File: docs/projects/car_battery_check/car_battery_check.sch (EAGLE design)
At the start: 18 parts, among them IC1 7805T, IC2 MEGA8-P

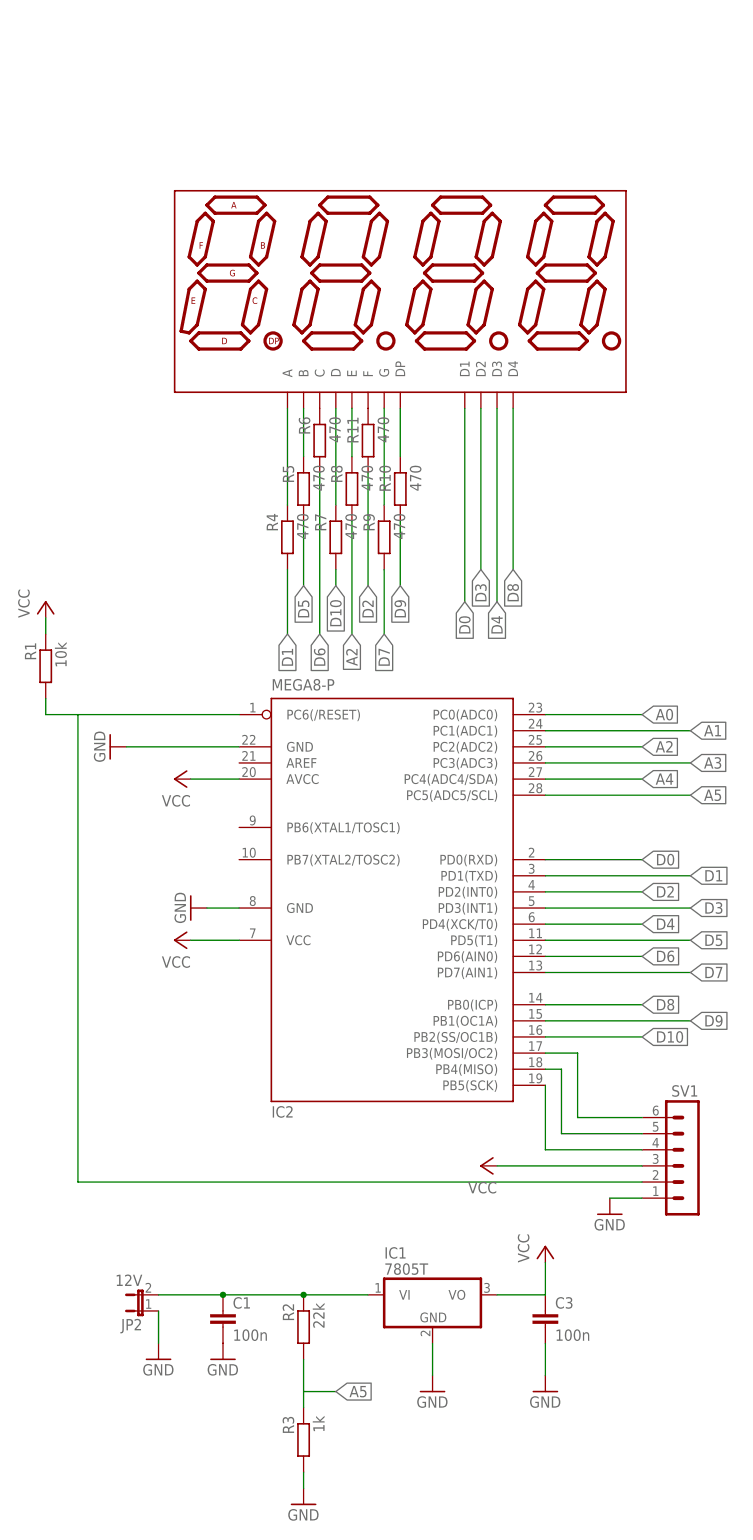
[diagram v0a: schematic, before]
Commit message: carbattery: adding voltage reference (MC1541)
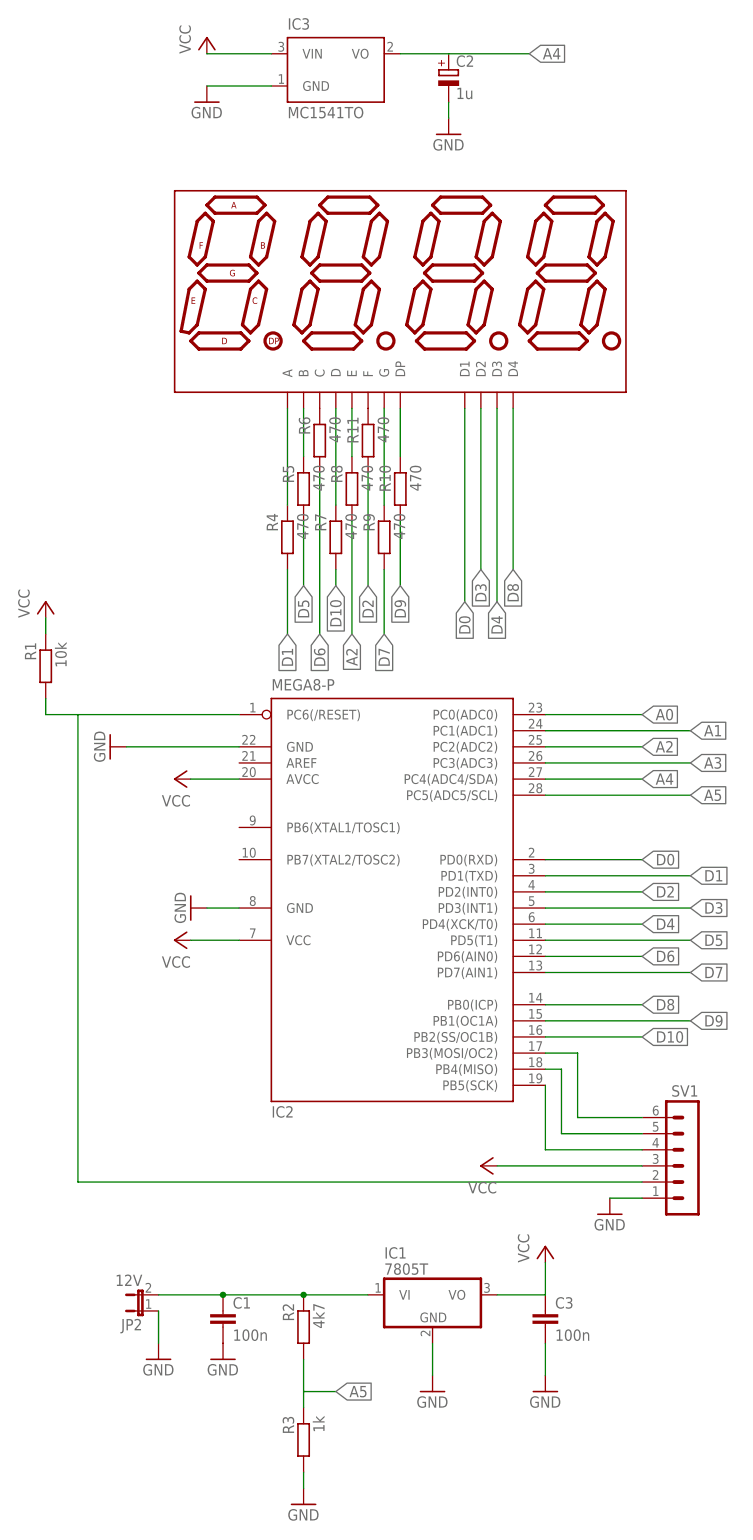
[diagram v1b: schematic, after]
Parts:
- added C2: 1u, rcl:CPOL-EUE2,5-6E
- added IC3: MC1541TO, microchip:MC1541TO
- R2: value 22k -> 4k7
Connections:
- net A4: now also C2.+, IC3.VO
- net GND: now also C2.-, IC3.GND
- net VCC: now also IC3.VIN
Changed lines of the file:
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@@
 <?xml version="1.0" encoding="utf-8"?>
 <!DOCTYPE eagle SYSTEM "eagle.dtd">
-<eagle version="6.2">
+<eagle version="6.4">
 <drawing>
 <settings>
@@
 <grid distance="0.1" unitdist="inch" unit="inch" style="lines" multiple="1" display="no" altdistance="0.01" altunitdist="inch" altunit="inch"/>
 <layers>
-<layer number="1" name="Top" color="4" fill="1" visible="yes" active="no"/>
-<layer number="16" name="Bottom" color="1" fill="1" visible="yes" active="no"/>
-<layer number="17" name="Pads" color="2" fill="1" visible="yes" active="no"/>
-<layer number="18" name="Vias" color="2" fill="1" visible="yes" active="no"/>
-<layer number="19" name="Unrouted" color="6" fill="1" visible="yes" active="no"/>
-<layer number="20" name="Dimension" color="15" fill="1" visible="yes" active="no"/>
-<layer number="21" name="tPlace" color="7" fill="1" visible="yes" active="no"/>
-<layer number="22" name="bPlace" color="7" fill="1" visible="yes" active="no"/>
-<layer number="23" name="tOrigins" color="15" fill="1" visible="yes" active="no"/>
-<layer number="24" name="bOrigins" color="15" fill="1" visible="yes" active="no"/>
-<layer number="25" name="tNames" color="7" fill="1" visible="yes" active="no"/>
-<layer number="26" name="bNames" color="7" fill="1" visible="yes" active="no"/>
-<layer number="27" name="tValues" color="7" fill="1" visible="yes" active="no"/>
-<layer number="28" name="bValues" color="7" fill="1" visible="yes" active="no"/>
+<layer number="1" name="Top" color="4" fill="1" visible="no" active="no"/>
+<layer number="16" name="Bottom" color="1" fill="1" visible="no" active="no"/>
+<layer number="17" name="Pads" color="2" fill="1" visible="no" active="no"/>
+<layer number="18" name="Vias" color="2" fill="1" visible="no" active="no"/>
+<layer number="19" name="Unrouted" color="6" fill="1" visible="no" active="no"/>
+<layer number="20" name="Dimension" color="15" fill="1" visible="no" active="no"/>
+<layer number="21" name="tPlace" color="7" fill="1" visible="no" active="no"/>
+<layer number="22" name="bPlace" color="7" fill="1" visible="no" active="no"/>
+<layer number="23" name="tOrigins" color="15" fill="1" visible="no" active="no"/>
+<layer number="24" name="bOrigins" color="15" fill="1" visible="no" active="no"/>
+<layer number="25" name="tNames" color="7" fill="1" visible="no" active="no"/>
+<layer number="26" name="bNames" color="7" fill="1" visible="no" active="no"/>
+<layer number="27" name="tValues" color="7" fill="1" visible="no" active="no"/>
+<layer number="28" name="bValues" color="7" fill="1" visible="no" active="no"/>
 <layer number="29" name="tStop" color="7" fill="3" visible="no" active="no"/>
 <layer number="30" name="bStop" color="7" fill="6" visible="no" active="no"/>
@@
 <layer number="35" name="tGlue" color="7" fill="4" visible="no" active="no"/>
 <layer number="36" name="bGlue" color="7" fill="5" visible="no" active="no"/>
-<layer number="37" name="tTest" color="7" fill="1" visible="yes" active="no"/>
-<layer number="38" name="bTest" color="7" fill="1" visible="yes" active="no"/>
+<layer number="37" name="tTest" color="7" fill="1" visible="no" active="no"/>
+<layer number="38" name="bTest" color="7" fill="1" visible="no" active="no"/>
 <layer number="39" name="tKeepout" color="4" fill="11" visible="no" active="no"/>
 <layer number="40" name="bKeepout" color="1" fill="11" visible="no" active="no"/>
@@
 <layer number="44" name="Drills" color="7" fill="1" visible="no" active="no"/>
 <layer number="45" name="Holes" color="7" fill="1" visible="no" active="no"/>
-<layer number="46" name="Milling" color="3" fill="1" visible="yes" active="no"/>
-<layer number="47" name="Measures" color="7" fill="1" visible="yes" active="no"/>
-<layer number="48" name="Document" color="7" fill="1" visible="yes" active="no"/>
-<layer number="49" name="Reference" color="7" fill="1" visible="yes" active="no"/>
-<layer number="50" name="dxf" color="7" fill="1" visible="yes" active="no"/>
-<layer number="51" name="tDocu" color="7" fill="1" visible="yes" active="no"/>
-<layer number="52" name="bDocu" color="7" fill="1" visible="yes" active="no"/>
-<layer number="53" name="tGND_GNDA" color="7" fill="9" visible="yes" active="no"/>
-<layer number="54" name="bGND_GNDA" color="1" fill="9" visible="yes" active="no"/>
-<layer number="56" name="wert" color="7" fill="1" visible="yes" active="no"/>
+<layer number="46" name="Milling" color="3" fill="1" visible="no" active="no"/>
+<layer number="47" name="Measures" color="7" fill="1" visible="no" active="no"/>
+<layer number="48" name="Document" color="7" fill="1" visible="no" active="no"/>
+<layer number="49" name="Reference" color="7" fill="1" visible="no" active="no"/>
+<layer number="50" name="dxf" color="7" fill="1" visible="no" active="no"/>
+<layer number="51" name="tDocu" color="7" fill="1" visible="no" active="no"/>
+<layer number="52" name="bDocu" color="7" fill="1" visible="no" active="no"/>
+<layer number="53" name="tGND_GNDA" color="7" fill="9" visible="no" active="no"/>
+<layer number="54" name="bGND_GNDA" color="1" fill="9" visible="no" active="no"/>
+<layer number="56" name="wert" color="7" fill="1" visible="no" active="no"/>
 <layer number="91" name="Nets" color="2" fill="1" visible="yes" active="yes"/>
 <layer number="92" name="Busses" color="1" fill="1" visible="yes" active="yes"/>
@@
 <part name="JP2" library="jumper" deviceset="JP1E" device="" value="12V"/>
 <part name="GND4" library="supply1" deviceset="GND" device=""/>
-<part name="R2" library="rcl" deviceset="R-EU_" device="R2512" value="22k"/>
+<part name="R2" library="rcl" deviceset="R-EU_" device="R2512" value="4k7"/>
 <part name="R3" library="rcl" deviceset="R-EU_" device="0207/15" value="1k"/>
 <part name="GND7" library="supply1" deviceset="GND" device=""/>
@@
 <part name="R10" library="rcl" deviceset="R-EU_" device="0204/7" value="470"/>
 <part name="R11" library="rcl" deviceset="R-EU_" device="0204/7" value="470"/>
+<part name="IC3" library="microchip" deviceset="MC15*" device="TO" technology="41"/>
+<part name="GND8" library="supply1" deviceset="GND" device=""/>
+<part name="P+2" library="supply1" deviceset="VCC" device=""/>
+<part name="C2" library="rcl" deviceset="CPOL-EU" device="E2,5-6E" value="1u"/>
+<part name="GND10" library="supply1" deviceset="GND" device=""/>
 </parts>
 <sheets>
@@
 <instance part="R10" gate="G$1" x="76.2" y="165.1" rot="MR270"/>
 <instance part="R11" gate="G$1" x="71.12" y="172.72" rot="MR270"/>
+<instance part="IC3" gate="G$1" x="66.04" y="231.14"/>
+<instance part="GND8" gate="1" x="45.72" y="226.06"/>
+<instance part="P+2" gate="VCC" x="45.72" y="236.22"/>
+<instance part="C2" gate="G$1" x="83.82" y="231.14"/>
+<instance part="GND10" gate="1" x="83.82" y="220.98"/>
 </instances>
 <busses>
@@
 <pinref part="GND5" gate="1" pin="GND"/>
 </segment>
+<segment>
+<pinref part="IC3" gate="G$1" pin="GND"/>
+<pinref part="GND8" gate="1" pin="GND"/>
+<wire x1="45.72" y1="228.6" x2="55.88" y2="228.6" width="0.1524" layer="91"/>
+</segment>
+<segment>
+<pinref part="C2" gate="G$1" pin="-"/>
+<pinref part="GND10" gate="1" pin="GND"/>
+<wire x1="83.82" y1="223.52" x2="83.82" y2="226.06" width="0.1524" layer="91"/>
+</segment>
 </net>
 <net name="VCC" class="0">
@@
 <pinref part="IC2" gate="G$1" pin="AVCC"/>
 <wire x1="43.18" y1="119.38" x2="50.8" y2="119.38" width="0.1524" layer="91"/>
+</segment>
+<segment>
+<pinref part="IC3" gate="G$1" pin="VIN"/>
+<pinref part="P+2" gate="VCC" pin="VCC"/>
+<wire x1="45.72" y1="233.68" x2="55.88" y2="233.68" width="0.1524" layer="91"/>
 </segment>
 </net>
@@
 <label x="114.3" y="119.38" size="1.778" layer="95" xref="yes"/>
 </segment>
-</net>
+<segment>
+<pinref part="IC3" gate="G$1" pin="VO"/>
+<pinref part="C2" gate="G$1" pin="+"/>
+<wire x1="83.82" y1="233.68" x2="76.2" y2="233.68" width="0.1524" layer="91"/>
+<wire x1="83.82" y1="233.68" x2="96.52" y2="233.68" width="0.1524" layer="91"/>
+<label x="96.52" y="233.68" size="1.778" layer="95" xref="yes"/>
+</segment>
+</net>
